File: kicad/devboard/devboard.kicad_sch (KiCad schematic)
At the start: 35 parts, among them J1 USB_C_Receptacle, J2 Conn_01x04_Socket, J3 Conn_02x03_Top_Bottom, J4 Conn_02x02_Top_Bottom, U1 LM3940, U2 CH340G, U3 STM32G030K8Tx, Y1 12 MHz, Y2 8 MHz

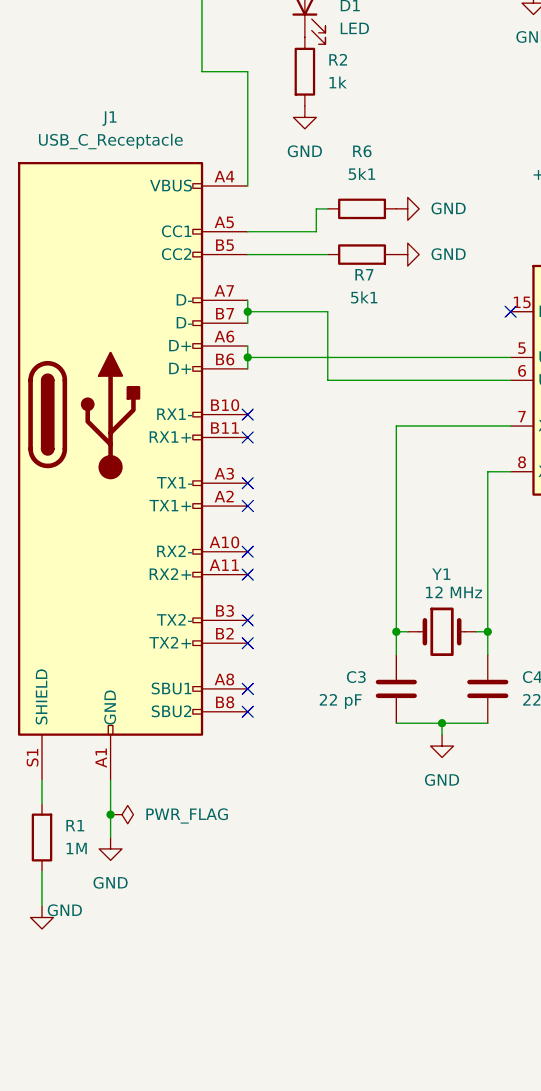
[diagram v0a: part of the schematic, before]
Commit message: Added new 16-pin USB C symbol, updated PCB
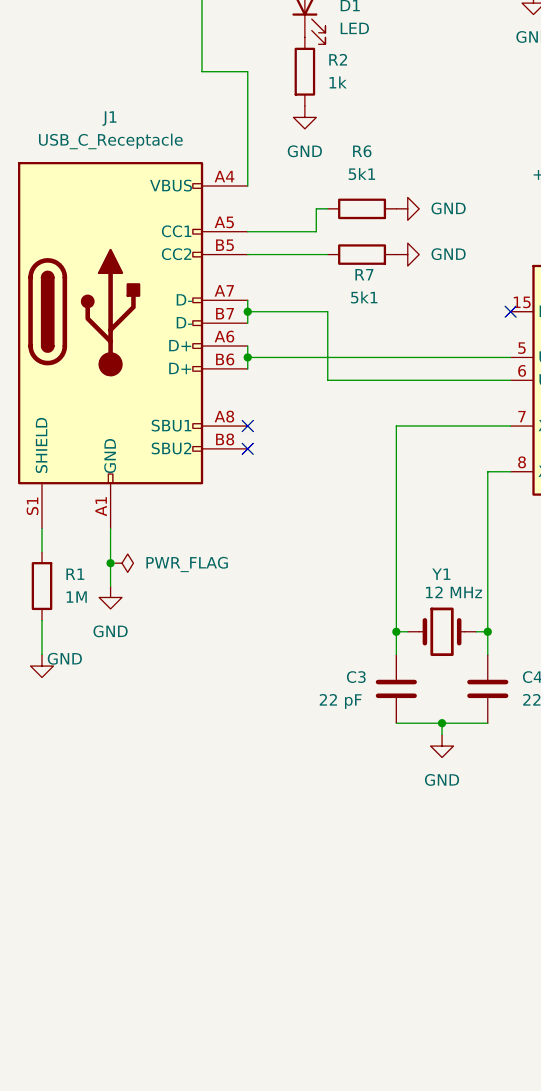
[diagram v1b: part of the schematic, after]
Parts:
- J1: symbol mesonlib:USB_C_Receptacle -> mesonlib:USB_C_Receptacle_16_pin
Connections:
- net GND: now also U1.4
- no-connect marks 33 -> 25
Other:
- moved on the sheet: R1
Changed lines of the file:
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@@
 	)
 	(junction
-		(at 29.21 134.62)
+		(at 29.21 106.68)
 		(diameter 0)
 		(color 0 0 0 0)
@@
 	)
 	(no_connect
-		(at 44.45 92.71)
+		(at 44.45 93.98)
 	)
 	(no_connect
-		(at 44.45 113.03)
-	)
-	(no_connect
-		(at 44.45 90.17)
+		(at 44.45 91.44)
 	)
 	(no_connect
@@
 	)
 	(no_connect
-		(at 44.45 100.33)
-	)
-	(no_connect
 		(at 73.66 78.74)
 	)
@@
 	)
 	(no_connect
-		(at 44.45 123.19)
-	)
-	(no_connect
 		(at 130.81 104.14)
 	)
@@
 	)
 	(no_connect
-		(at 44.45 120.65)
-	)
-	(no_connect
-		(at 44.45 97.79)
-	)
-	(no_connect
-		(at 44.45 107.95)
-	)
-	(no_connect
-		(at 44.45 115.57)
-	)
-	(no_connect
 		(at 130.81 109.22)
 	)
@@
 	)
 	(no_connect
-		(at 44.45 105.41)
-	)
-	(no_connect
 		(at 93.98 93.98)
 	)
@@
 	(wire
 		(pts
-			(xy 29.21 130.81) (xy 29.21 134.62)
+			(xy 29.21 102.87) (xy 29.21 106.68)
 		)
 		(stroke
@@
 	(wire
 		(pts
-			(xy 21.59 140.97) (xy 21.59 144.78)
+			(xy 21.59 113.03) (xy 21.59 116.84)
 		)
 		(stroke
@@
 	(wire
 		(pts
-			(xy 29.21 134.62) (xy 29.21 137.16)
+			(xy 29.21 106.68) (xy 29.21 109.22)
 		)
 		(stroke
@@
 	(wire
 		(pts
-			(xy 21.59 130.81) (xy 21.59 133.35)
+			(xy 21.59 102.87) (xy 21.59 105.41)
 		)
 		(stroke
@@
 	)
 	(symbol
-		(lib_id "mesonlib:USB_C_Receptacle")
+		(lib_id "mesonlib:USB_C_Receptacle_16_pin")
 		(at 29.21 90.17 0)
 		(unit 1)
@@
 		)
 		(property "Datasheet" "https://www.usb.org/sites/default/files/documents/usb_type-c.zip"
-			(at 33.02 90.17 0)
+			(at 33.02 91.948 0)
 			(effects
 				(font
@@
 		)
 		(property "Description" "USB Full-Featured Type-C Receptacle connector"
-			(at 29.21 90.17 0)
+			(at 29.21 89.154 0)
 			(effects
 				(font
@@
 		(pin "S1"
 		)
-		(pin "B11"
-		)
-		(pin "B10"
-		)
 		(pin "A8"
 		)
@@
 		(pin "A4"
 		)
-		(pin "A2"
-		)
-		(pin "A3"
-		)
 		(pin "A1"
 		)
@@
 		(pin "A12"
 		)
-		(pin "B2"
-		)
 		(pin "B6"
 		)
@@
 		(pin "B8"
 		)
-		(pin "B3"
-		)
 		(pin "B9"
 		)
-		(pin "A11"
-		)
 		(pin "B1"
 		)
 		(pin "B12"
 		)
-		(pin "A10"
-		)
 		(pin "B7"
 		)
@@
 	(symbol
 		(lib_id "power:GND")
-		(at 29.21 137.16 0)
+		(at 29.21 109.22 0)
 		(unit 1)
 		(exclude_from_sim no)
@@
 		(fields_autoplaced yes)
 		(property "Reference" "#PWR02"
-			(at 29.21 143.51 0)
+			(at 29.21 115.57 0)
 			(effects
 				(font
@@
 		)
 		(property "Value" "GND"
-			(at 29.21 142.24 0)
+			(at 29.21 114.3 0)
 			(effects
 				(font
@@
 		)
 		(property "Footprint" ""
-			(at 29.21 137.16 0)
+			(at 29.21 109.22 0)
 			(effects
 				(font
@@
 		)
 		(property "Datasheet" ""
-			(at 29.21 137.16 0)
+			(at 29.21 109.22 0)
 			(effects
 				(font
@@
 		)
 		(property "Description" "Power symbol creates a global label with name \"GND\" , ground"
-			(at 29.21 137.16 0)
+			(at 29.21 109.22 0)
 			(effects
 				(font
@@
 	(symbol
 		(lib_id "Device:R")
-		(at 21.59 137.16 180)
+		(at 21.59 109.22 180)
 		(unit 1)
 		(exclude_from_sim no)
@@
 		(fields_autoplaced yes)
 		(property "Reference" "R1"
-			(at 24.13 135.8899 0)
+			(at 24.13 107.9499 0)
 			(effects
 				(font
@@
 		)
 		(property "Value" "1M"
-			(at 24.13 138.4299 0)
+			(at 24.13 110.4899 0)
 			(effects
 				(font
@@
 		)
 		(property "Footprint" "Resistor_SMD:R_0603_1608Metric"
-			(at 23.368 137.16 90)
+			(at 23.368 109.22 90)
 			(effects
 				(font
@@
 		)
 		(property "Datasheet" "~"
-			(at 21.59 137.16 0)
+			(at 21.59 109.22 0)
 			(effects
 				(font
@@
 		)
 		(property "Description" "Resistor"
-			(at 21.59 137.16 0)
+			(at 21.59 109.22 0)
 			(effects
 				(font
@@
 	(symbol
 		(lib_id "power:GND")
-		(at 21.59 144.78 0)
+		(at 21.59 116.84 0)
 		(unit 1)
 		(exclude_from_sim no)
@@
 		(dnp no)
 		(property "Reference" "#PWR01"
-			(at 21.59 151.13 0)
+			(at 21.59 123.19 0)
 			(effects
 				(font
@@
 		)
 		(property "Value" "GND"
-			(at 24.13 145.288 0)
+			(at 24.13 117.348 0)
 			(effects
 				(font
@@
 		)
 		(property "Footprint" ""
-			(at 21.59 144.78 0)
+			(at 21.59 116.84 0)
 			(effects
 				(font
@@
 		)
 		(property "Datasheet" ""
-			(at 21.59 144.78 0)
+			(at 21.59 116.84 0)
 			(effects
 				(font
@@
 		)
 		(property "Description" "Power symbol creates a global label with name \"GND\" , ground"
-			(at 21.59 144.78 0)
+			(at 21.59 116.84 0)
 			(effects
 				(font
@@
 	(symbol
 		(lib_id "power:PWR_FLAG")
-		(at 29.21 134.62 270)
+		(at 29.21 106.68 270)
 		(unit 1)
 		(exclude_from_sim no)
@@
 		(fields_autoplaced yes)
 		(property "Reference" "#FLG02"
-			(at 31.115 134.62 0)
+			(at 31.115 106.68 0)
 			(effects
 				(font
@@
 		)
 		(property "Value" "PWR_FLAG"
-			(at 33.02 134.6199 90)
+			(at 33.02 106.6799 90)
 			(effects
 				(font
@@
 		)
 		(property "Footprint" ""
-			(at 29.21 134.62 0)
+			(at 29.21 106.68 0)
 			(effects
 				(font
@@
 		)
 		(property "Datasheet" "~"
-			(at 29.21 134.62 0)
+			(at 29.21 106.68 0)
 			(effects
 				(font
@@
 		)
 		(property "Description" "Special symbol for telling ERC where power comes from"
-			(at 29.21 134.62 0)
+			(at 29.21 106.68 0)
 			(effects
 				(font
@@
 		(pin "1"
 		)
+		(pin "4"
+		)
 		(instances

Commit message: Added 3pad resistor comment, and spread the board out
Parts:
- removed J3: Conn_02x03_Top_Bottom, Connector_PinHeader_2.54mm:PinHeader_2x03_P2.54mm_Vertical, symbol Connector_Generic:Conn_02x03_Top_Bottom
- removed R8, R9: 1k, Resistor_SMD:R_0603_1608Metric, symbol Device:R
- added R5, R6: 1k, mesonlib:resistor_3pad_switch_0603, symbol mesonlib:resistor_3pad_switch
- renumbered C3 to C2, C4 to C3, C9 to C4, C7 to C5, C5 to C6, C8 to C7, C6 to C8, J4 to J2, J2 to J3, R11 to R10, R10 to R11, R6 to R3, R7 to R4, R5 to R7, R3 to R8, R4 to R9
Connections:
- net RX-M: now also R5.3 (R), R6.3 (R)
- net RX-U: now also U2.3 (RXD), R6.2 (C)
- net TX-M: now also R5.1 (L), R6.1 (L)
- net TX-U: now also U2.2 (TXD), R5.2 (C)

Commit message: Added MOSFET to drive LEDs
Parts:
- added Q1: BSS138, Package_TO_SOT_SMD:SOT-23, symbol Transistor_FET:BSS138
- added R12: 10k, symbol Device:R
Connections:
- net +5V: now also R12.1
- net GND: now also Q1.2 (S)
- net at D2.3 (DIN): now also Q1.3 (D), R12.2; no longer U3.7 (PA0)
- new net: Q1.1 (G), U3.7 (PA0)
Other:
- moved on the sheet: R5, R6

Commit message: Added most routing, besides the debug header
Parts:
- R12: footprint (none) -> Resistor_SMD:R_0603_1608Metric
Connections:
- net +3.3V: now also J2.1 (Pin_1); no longer J2.3 (Pin_3)
- net GND: now also J2.3 (Pin_3); no longer J2.4 (Pin_4)
- net I2C1_SCL: now also J3.2 (Pin_2); no longer J3.3 (Pin_3)
- net I2C1_SDA: now also J3.3 (Pin_3); no longer J3.2 (Pin_2)
- net SWCLK/BOOT: now also J2.4 (Pin_4); no longer J2.2 (Pin_2)
- net SWDIO: now also J2.2 (Pin_2); no longer J2.1 (Pin_1)
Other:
- moved on the sheet: J2, R10
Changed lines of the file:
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@@
 	)
 	(junction
-		(at 219.71 123.19)
+		(at 217.17 134.62)
 		(diameter 0)
 		(color 0 0 0 0)
@@
 	)
 	(junction
+		(at 217.17 142.24)
+		(diameter 0)
+		(color 0 0 0 0)
+	)
+	(junction
 		(at 143.51 120.65)
 		(diameter 0)
@@
 	(wire
 		(pts
+			(xy 217.17 142.24) (xy 223.52 142.24)
+		)
+		(stroke
+			(width 0)
+			(type default)
+		)
+	)
+	(wire
+		(pts
 			(xy 60.96 124.46) (xy 66.04 124.46)
 		)
@@
 	(wire
 		(pts
-			(xy 209.55 123.19) (xy 219.71 123.19)
+			(xy 203.2 142.24) (xy 217.17 142.24)
 		)
 		(stroke
@@
 	(wire
 		(pts
-			(xy 223.52 124.46) (xy 223.52 123.19)
+			(xy 223.52 140.97) (xy 223.52 142.24)
 		)
 		(stroke
@@
 	(wire
 		(pts
-			(xy 219.71 123.19) (xy 223.52 123.19)
-		)
-		(stroke
-			(width 0)
-			(type default)
-		)
-	)
-	(wire
-		(pts
 			(xy 158.75 106.68) (xy 175.26 106.68)
 		)
@@
 	(wire
 		(pts
-			(xy 237.49 127) (xy 236.22 127)
+			(xy 236.22 138.43) (xy 238.76 138.43)
+		)
+		(stroke
+			(width 0)
+			(type default)
+		)
+	)
+	(wire
+		(pts
+			(xy 222.25 138.43) (xy 223.52 138.43)
+		)
+		(stroke
+			(width 0)
+			(type default)
+		)
+	)
+	(wire
+		(pts
+			(xy 217.17 134.62) (xy 222.25 134.62)
 		)
 		(stroke
@@
 	(wire
 		(pts
-			(xy 237.49 128.27) (xy 237.49 127)
-		)
-		(stroke
-			(width 0)
-			(type default)
-		)
-	)
-	(wire
-		(pts
 			(xy 113.03 111.76) (xy 113.03 162.56)
 		)
@@
 	(wire
 		(pts
-			(xy 238.76 128.27) (xy 237.49 128.27)
-		)
-		(stroke
-			(width 0)
-			(type default)
-		)
-	)
-	(wire
-		(pts
 			(xy 219.71 50.8) (xy 219.71 54.61)
 		)
@@
 	(wire
 		(pts
-			(xy 238.76 124.46) (xy 236.22 124.46)
+			(xy 222.25 134.62) (xy 222.25 138.43)
+		)
+		(stroke
+			(width 0)
+			(type default)
+		)
+	)
+	(wire
+		(pts
+			(xy 212.09 134.62) (xy 217.17 134.62)
 		)
 		(stroke
@@
 	(wire
 		(pts
-			(xy 223.52 127) (xy 223.52 128.27)
+			(xy 236.22 140.97) (xy 236.22 142.24)
 		)
 		(stroke
@@
 	(wire
 		(pts
-			(xy 209.55 128.27) (xy 223.52 128.27)
+			(xy 250.19 142.24) (xy 236.22 142.24)
 		)
 		(stroke
@@
 	)
 	(label "SWCLK{slash}BOOT"
-		(at 209.55 128.27 0)
+		(at 250.19 142.24 180)
 		(fields_autoplaced yes)
 		(effects
@@
 				(size 1.27 1.27)
 			)
-			(justify left bottom)
+			(justify right bottom)
 		)
 	)
@@
 	)
 	(label "SWDIO"
-		(at 209.55 123.19 0)
+		(at 203.2 142.24 0)
 		(fields_autoplaced yes)
 		(effects
@@
 		)
 	)
-	(label "I2C1_SDA"
+	(label "I2C1_SCL"
 		(at 228.6 96.52 0)
 		(fields_autoplaced yes)
@@
 		)
 	)
-	(label "I2C1_SCL"
+	(label "I2C1_SDA"
 		(at 228.6 99.06 0)
 		(fields_autoplaced yes)
@@
 			)
 		)
-		(property "Footprint" ""
+		(property "Footprint" "Resistor_SMD:R_0603_1608Metric"
 			(at 118.872 153.67 90)
 			(effects
@@
 	(symbol
 		(lib_id "Connector_Generic:Conn_02x02_Top_Bottom")
-		(at 228.6 124.46 0)
+		(at 228.6 138.43 0)
 		(unit 1)
 		(exclude_from_sim no)
@@
 		(dnp no)
 		(property "Reference" "J2"
-			(at 229.87 118.11 0)
+			(at 229.87 132.08 0)
 			(effects
 				(font
@@
 		)
 		(property "Value" "Conn_02x02_Top_Bottom"
-			(at 240.538 120.65 0)
+			(at 240.538 134.62 0)
 			(effects
 				(font
@@
 		)
 		(property "Footprint" "Connector_PinHeader_2.54mm:PinHeader_2x02_P2.54mm_Vertical"
-			(at 228.6 124.46 0)
+			(at 228.6 138.43 0)
 			(effects
 				(font
@@
 		)
 		(property "Datasheet" "~"
-			(at 228.6 124.46 0)
+			(at 228.6 138.43 0)
 			(effects
 				(font
@@
 		)
 		(property "Description" "Generic connector, double row, 02x02, top/bottom pin numbering scheme (row 1: 1...pins_per_row, row2: pins_per_row+1 ... num_pins), script generated (kicad-library-utils/schlib/autogen/connector/)"
-			(at 228.6 124.46 0)
+			(at 228.6 138.43 0)
 			(effects
 				(font
@@
 	(symbol
 		(lib_id "Device:R")
-		(at 219.71 119.38 0)
+		(at 217.17 138.43 0)
 		(unit 1)
 		(exclude_from_sim no)
@@
 		(on_board yes)
 		(dnp no)
-		(fields_autoplaced yes)
 		(property "Reference" "R10"
-			(at 222.25 118.1099 0)
+			(at 214.63 137.1599 0)
 			(effects
 				(font
 					(size 1.27 1.27)
 				)
-				(justify left)
+				(justify right)
 			)
 		)
 		(property "Value" "10k"
-			(at 222.25 120.6499 0)
+			(at 214.63 139.6999 0)
 			(effects
 				(font
 					(size 1.27 1.27)
 				)
-				(justify left)
+				(justify right)
 			)
 		)
 		(property "Footprint" "Resistor_SMD:R_0603_1608Metric"
-			(at 217.932 119.38 90)
+			(at 215.392 138.43 90)
 			(effects
 				(font
@@
 		)
 		(property "Datasheet" "~"
-			(at 219.71 119.38 0)
+			(at 217.17 138.43 0)
 			(effects
 				(font
@@
 		)
 		(property "Description" "Resistor"
-			(at 219.71 119.38 0)
+			(at 217.17 138.43 0)
 			(effects
 				(font
@@
 	(symbol
 		(lib_id "power:+3.3V")
-		(at 219.71 115.57 0)
-		(unit 1)
-		(exclude_from_sim no)
-		(in_bom yes)
-		(on_board yes)
-		(dnp no)
-		(fields_autoplaced yes)
-		(property "Reference" "#PWR026"
-			(at 219.71 119.38 0)
-			(effects
-				(font
-					(size 1.27 1.27)
-				)
-				(hide yes)
-			)
-		)
-		(property "Value" "+3.3V"
-			(at 219.71 110.49 0)
-			(effects
-				(font
-					(size 1.27 1.27)
-				)
-			)
-		)
-		(property "Footprint" ""
-			(at 219.71 115.57 0)
-			(effects
-				(font
-					(size 1.27 1.27)
-				)
-				(hide yes)
-			)
-		)
-		(property "Datasheet" ""
-			(at 219.71 115.57 0)
-			(effects
-				(font
-					(size 1.27 1.27)
-				)
-				(hide yes)
-			)
-		)
-		(property "Description" "Power symbol creates a global label with name \"+3.3V\""
-			(at 219.71 115.57 0)
-			(effects
-				(font
-					(size 1.27 1.27)
-				)
-				(hide yes)
-			)
-		)
-		(pin "1"
-		)
-		(instances
-			(project "devboard"
-				(path "/c3bd2aeb-acec-4e93-ab92-7a030f22ab8b"
-					(reference "#PWR026")
-					(unit 1)
-				)
-			)
-		)
-	)
-	(symbol
-		(lib_id "power:+3.3V")
-		(at 238.76 124.46 270)
+		(at 212.09 134.62 90)
 		(unit 1)
 		(exclude_from_sim no)
@@
 		(fields_autoplaced yes)
 		(property "Reference" "#PWR029"
-			(at 234.95 124.46 0)
+			(at 215.9 134.62 0)
 			(effects
 				(font
@@
 		)
 		(property "Value" "+3.3V"
-			(at 242.57 124.4599 90)
+			(at 208.28 134.6201 90)
 			(effects
 				(font
@@
 		)
 		(property "Footprint" ""
-			(at 238.76 124.46 0)
+			(at 212.09 134.62 0)
 			(effects
 				(font
@@
 		)
 		(property "Datasheet" ""
-			(at 238.76 124.46 0)
+			(at 212.09 134.62 0)
 			(effects
 				(font
@@
 		)
 		(property "Description" "Power symbol creates a global label with name \"+3.3V\""
-			(at 238.76 124.46 0)
+			(at 212.09 134.62 0)
 			(effects
 				(font
@@
 	(symbol
 		(lib_id "power:GND")
-		(at 238.76 128.27 90)
+		(at 238.76 138.43 90)
 		(unit 1)
 		(exclude_from_sim no)
@@
 		(fields_autoplaced yes)
 		(property "Reference" "#PWR030"
-			(at 245.11 128.27 0)
+			(at 245.11 138.43 0)
 			(effects
 				(font
@@
 		)
 		(property "Value" "GND"
-			(at 242.57 128.2699 90)
+			(at 242.57 138.4299 90)
 			(effects
 				(font
@@
 		)
 		(property "Footprint" ""
-			(at 238.76 128.27 0)
+			(at 238.76 138.43 0)
 			(effects
 				(font
@@
 		)
 		(property "Datasheet" ""
-			(at 238.76 128.27 0)
+			(at 238.76 138.43 0)
 			(effects
 				(font
@@
 		)
 		(property "Description" "Power symbol creates a global label with name \"GND\" , ground"
-			(at 238.76 128.27 0)
+			(at 238.76 138.43 0)
 			(effects
 				(font

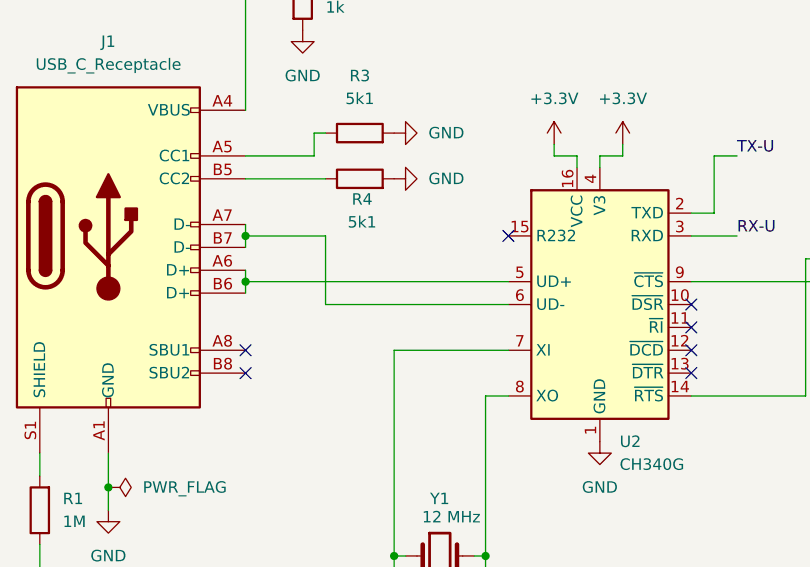
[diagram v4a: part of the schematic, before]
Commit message: Fixed USB routing, simplified other routes
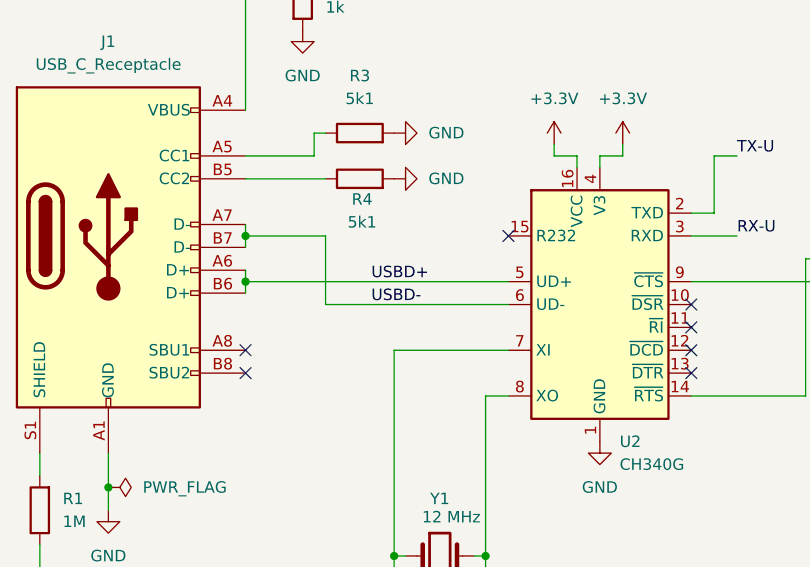
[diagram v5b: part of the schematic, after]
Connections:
- net USBD+: now reaches J1.A6 (D+), J1.B6 (D+), U2.5 (UD+)
- net USBD-: now reaches J1.A7 (D-), J1.B7 (D-), U2.6 (UD-)
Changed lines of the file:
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@@
+		)
+	)
+	(label "USBD+"
+		(at 58.42 83.82 0)
+		(fields_autoplaced yes)
+		(effects
+			(font
+				(size 1.27 1.27)
+			)
+			(justify left bottom)
 		)
 	)
@@
 		(fields_autoplaced yes)
 		(effects
+			(font
+				(size 1.27 1.27)
+			)
+			(justify left bottom)
+		)
+	)
+	(label "USBD-"
+		(at 58.42 86.36 0)
+		(fields_autoplaced yes)
+		(effects

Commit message: Finalized, fixing all ERC and DRC warnings
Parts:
- J1: footprint Connector_USB:USB_C_Receptacle_Palconn_UTC16-G -> mesonlib:USB_C_Receptacle_Palconn_UTC16-G_pcb_edge
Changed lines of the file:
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@@
 			)
 		)
-		(property "Footprint" "Connector_USB:USB_C_Receptacle_Palconn_UTC16-G"
+		(property "Footprint" "mesonlib:USB_C_Receptacle_Palconn_UTC16-G_pcb_edge"
 			(at 33.02 90.17 0)
 			(effects

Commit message: final fixes
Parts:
- C8: value 0.1 uF -> 100 nF
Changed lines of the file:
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@@
 			)
 		)
-		(property "Value" "0.1 uF"
+		(property "Value" "100 nF"
 			(at 257.81 57.1499 0)
 			(effects
